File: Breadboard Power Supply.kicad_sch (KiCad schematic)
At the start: 28 parts, among them J1 USB-C, J10 Conn_01x02_Male, J11 Conn_01x02_Male, J2 Conn_02x03_Odd_Even, J3 Conn_02x03_Odd_Even, J8 Conn_01x02_Male, J9 Conn_01x02_Male, U1 LM1117DT-ADJ, U2 LM1117DT-ADJ

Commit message: Updated potentiometer part number.
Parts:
- RV1, RV2: Digi-Key Part Num (none) -> 563-ST4ETB102CT-ND; Manufacturer (none) -> Nidec; Mfg Part Num (none) -> ST-4ETB102
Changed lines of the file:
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@@
       (effects (font (size 1.27 1.27)) hide)
     )
-    (property "Datasheet" "~" (at 97.79 106.68 0)
-      (effects (font (size 1.27 1.27)) hide)
+    (property "Datasheet" "https://www.nidec-components.com/e/catalog/trimmer/st-4.pdf" (at 97.79 106.68 0)
+      (effects (font (size 1.27 1.27)) hide)
+    )
+    (property "Manufacturer" "Nidec" (at 97.79 106.68 0)
+      (effects (font (size 1.27 1.27)) hide)
+    )
+    (property "Mfg Part Num" "ST-4ETB102" (at 97.79 106.68 0)
+      (effects (font (size 1.27 1.27)) hide)
+    )
+    (property "Digi-Key Part Num" "563-ST4ETB102CT-ND" (at 97.79 106.68 0)
+      (effects (font (size 1.27 1.27)) hide)
+    )
+    (property "Description" "" (at 97.79 106.68 0)
+      (effects (font (size 1.27 1.27)))
     )
     (pin "1")
@@
       (effects (font (size 1.27 1.27)) hide)
     )
-    (property "Datasheet" "~" (at 97.79 151.13 0)
-      (effects (font (size 1.27 1.27)) hide)
-    )
-    (pin "1")
+    (property "Datasheet" "https://www.nidec-components.com/e/catalog/trimmer/st-4.pdf" (at 97.79 151.13 0)
+      (effects (font (size 1.27 1.27)) hide)
+    )
+    (property "Manufacturer" "Nidec" (at 97.79 151.13 0)
+      (effects (font (size 1.27 1.27)) hide)
+    )
+    (property "Mfg Part Num" "ST-4ETB102" (at 97.79 151.13 0)
+      (effects (font (size 1.27 1.27)) hide)
+    )
+    (property "Digi-Key Part Num" "563-ST4ETB102CT-ND" (at 97.79 151.13 0)
+      (effects (font (size 1.27 1.27)) hide)
+    )
+    (property "Description" "" (at 97.79 151.13 0)
+      (effects (font (size 1.27 1.27)))
+    )
+    (pin "1")

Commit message: Got rid of To Do list.
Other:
- note removed: "To Do 1) XXX Move the R1 reference designator away from the USB-C mounting hole. 2) XXX Use variable voltage regulators. 3) XXX Update version numbers. 4) XXX Get rid of local libraries. 5) XXX Doublecheck fill areas. 6) Finish mechanical changes. 7) XXX Change the order of the power headers. 8) XXX Get rid of the Zener diode. 9) XXX There's a via in the word Supply on the back silkscreen."
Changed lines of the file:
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@@
     (effects (font (size 1.27 1.27)) (justify left bottom))
-  )
-  (text "To Do\n\n1) XXX Move the R1 reference designator away from the USB-C mounting hole.\n2) XXX Use variable voltage regulators.\n3) XXX Update version numbers.\n4) XXX Get rid of local libraries.\n5) XXX Doublecheck fill areas.\n6) Finish mechanical changes.\n7) XXX Change the order of the power headers.\n8) XXX Get rid of the Zener diode.\n9) XXX There's a via in the word Supply on the back silkscreen."
-    (at 172.72 46.99 0)
-    (effects (font (size 1.27 1.27)) (justify left bottom) (href "#1"))
   )
   (text "5V Input" (at 50.8 24.765 0)

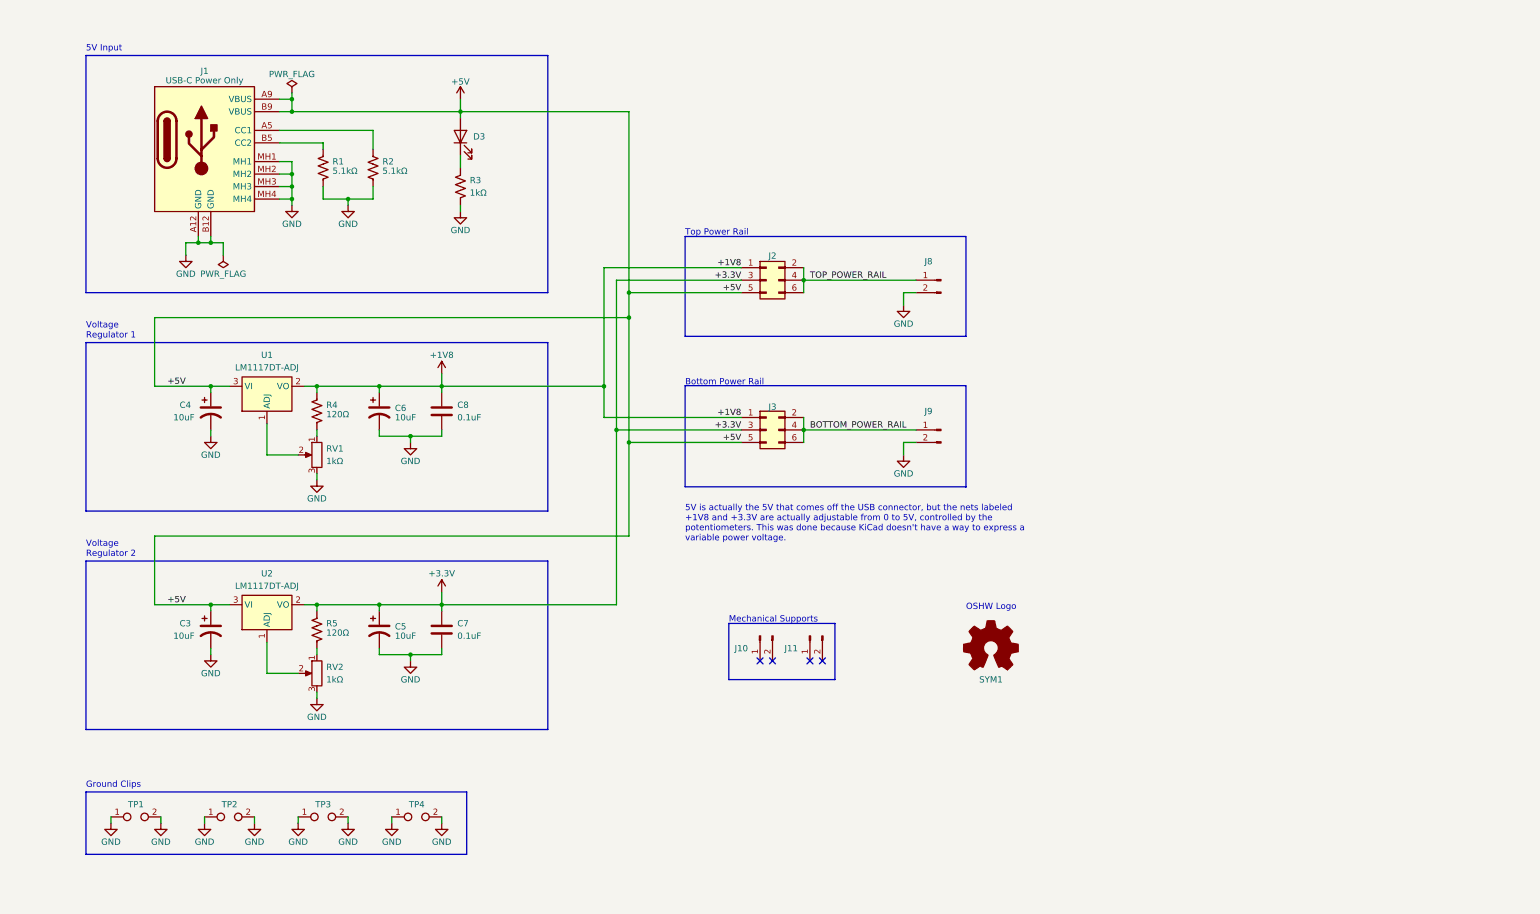
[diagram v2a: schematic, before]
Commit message: Redid schematic with both fixed and adjustable voltage regulators.
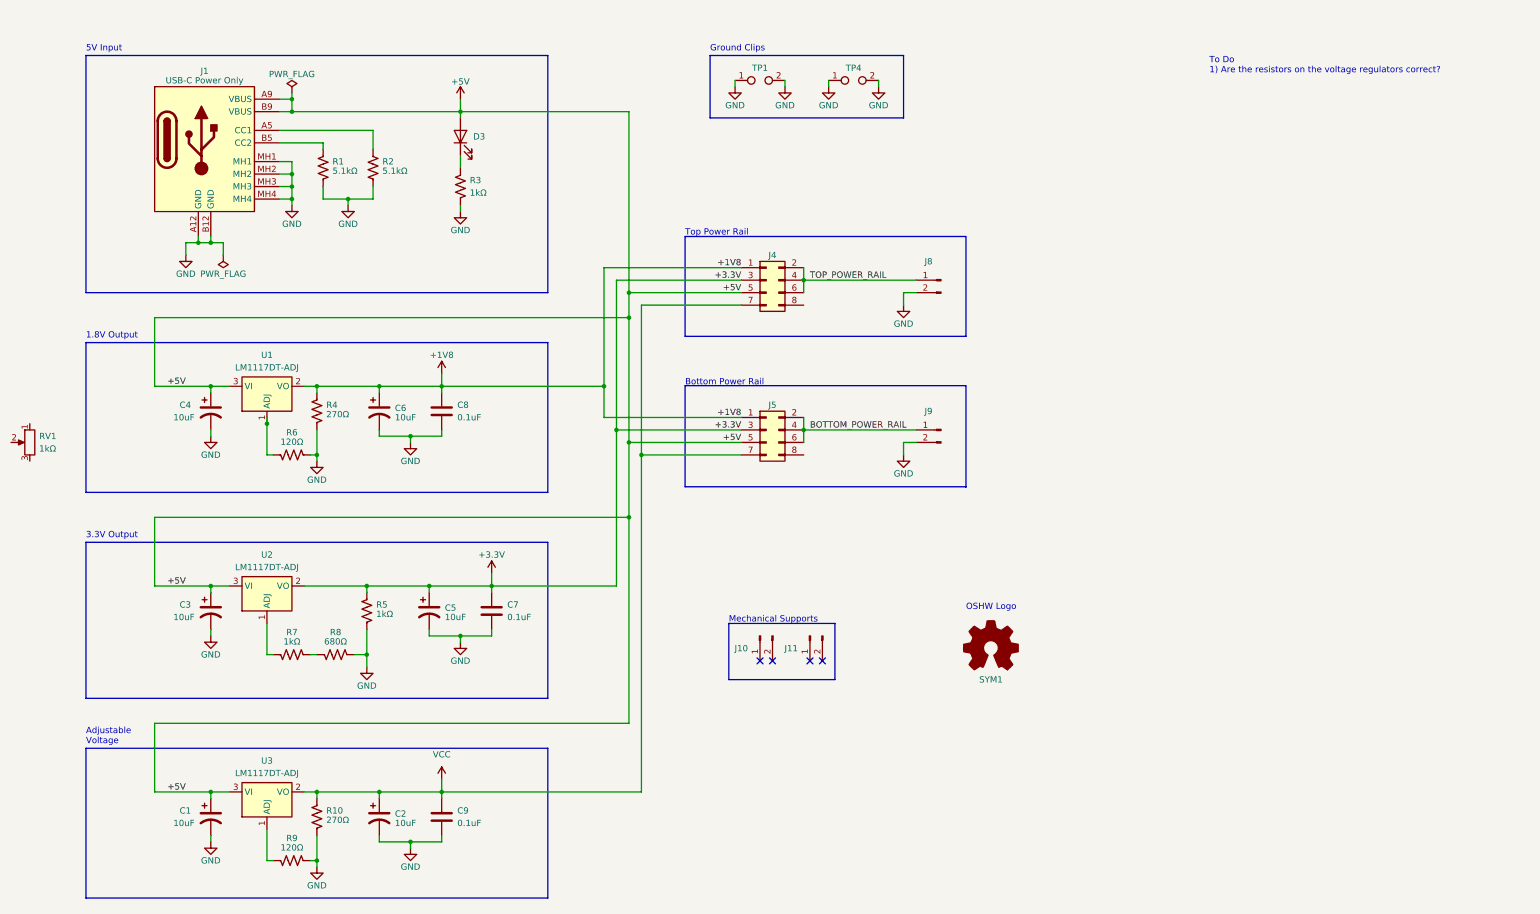
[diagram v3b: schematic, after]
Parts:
- removed J2, J3: Conn_02x03_Odd_Even, Connector_PinHeader_2.54mm:PinHeader_2x03_P2.54mm_Vertical, symbol Connector_Generic:Conn_02x03_Odd_Even
- removed RV2: 1kΩ, Local-Footprints:ST4ETB103 Potentiometer, symbol Device:R_Potentiometer
- removed TP2, TP3: TestPoint_2Pole, Global-Footprints:Keystone 1430, symbol Connector:TestPoint_2Pole
- added C1, C2: 10uF, Capacitor_SMD:C_0805_2012Metric, symbol Device:C_Polarized_US
- added C9: 0.1uF, Capacitor_SMD:C_0402_1005Metric, symbol Device:C
- added J4, J5: Conn_02x04_Odd_Even, Connector_PinHeader_2.54mm:PinHeader_2x04_P2.54mm_Vertical, symbol Connector_Generic:Conn_02x04_Odd_Even
- added R10: 270Ω, Resistor_SMD:R_0402_1005Metric, symbol Device:R_US
- added R6, R9: 120Ω, Resistor_SMD:R_0402_1005Metric, symbol Device:R_US
- added R7: 1kΩ, Resistor_SMD:R_0402_1005Metric, symbol Device:R_US
- added R8: 680Ω, Resistor_SMD:R_0402_1005Metric, symbol Device:R_US
- added U3: LM1117DT-ADJ, Package_TO_SOT_SMD:SOT-223-3_TabPin2, symbol Regulator_Linear:LM1117DT-ADJ
- R4: value 120Ω -> 270Ω
- R5: value 120Ω -> 1kΩ
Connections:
- net +1V8: now also J4.1 (Pin_1), J5.1 (Pin_1)
- net +3.3V: now also J4.3 (Pin_3), J5.3 (Pin_3)
- net +5V: now also C1.1, J4.5 (Pin_5), J5.5 (Pin_5), U3.3 (VI)
- net BOTTOM_POWER_RAIL: now also J5.2 (Pin_2), J5.4 (Pin_4), J5.6 (Pin_6)
- net GND: now also R4.2, R5.2, C1.2, C2.2, C9.2, R10.2, R6.2, R8.2, R9.2; no longer RV1.3
- net TOP_POWER_RAIL: now also J4.2 (Pin_2), J4.4 (Pin_4), J4.6 (Pin_6)
- net at RV1.1: no longer R4.2
- net at RV1.2: no longer U1.1 (ADJ)
- net at U2.1 (ADJ): now also R7.1
- new net: R6.1, U1.1 (ADJ)
- new net: R7.2, R8.1
- new net: R9.1, U3.1 (ADJ)
- new net VCC: C2.1, C9.1, J4.7 (Pin_7), J5.7 (Pin_7), R10.1, U3.2 (VO)
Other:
- note added: "1.8V Output"
- note added: "3.3V Output"
- note added: "Adjustable Voltage"
- note added: "To Do 1) Are the resistors on the voltage regulators correct?"
- note removed: "5V is actually the 5V that comes off the USB connector, but the nets labeled +1V8 and +3.3V are actually adjustable from 0 to 5V, controlled by the potentiometers. This was done because KiCad doesn't have a way to express a variable power voltage."
- note removed: "Voltage Regulator 1"
- note removed: "Voltage Regulator 2"
- moved on the sheet: C3, C5, C7, R5, RV1, TP1, TP4, U2

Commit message: Feature complete schematic.
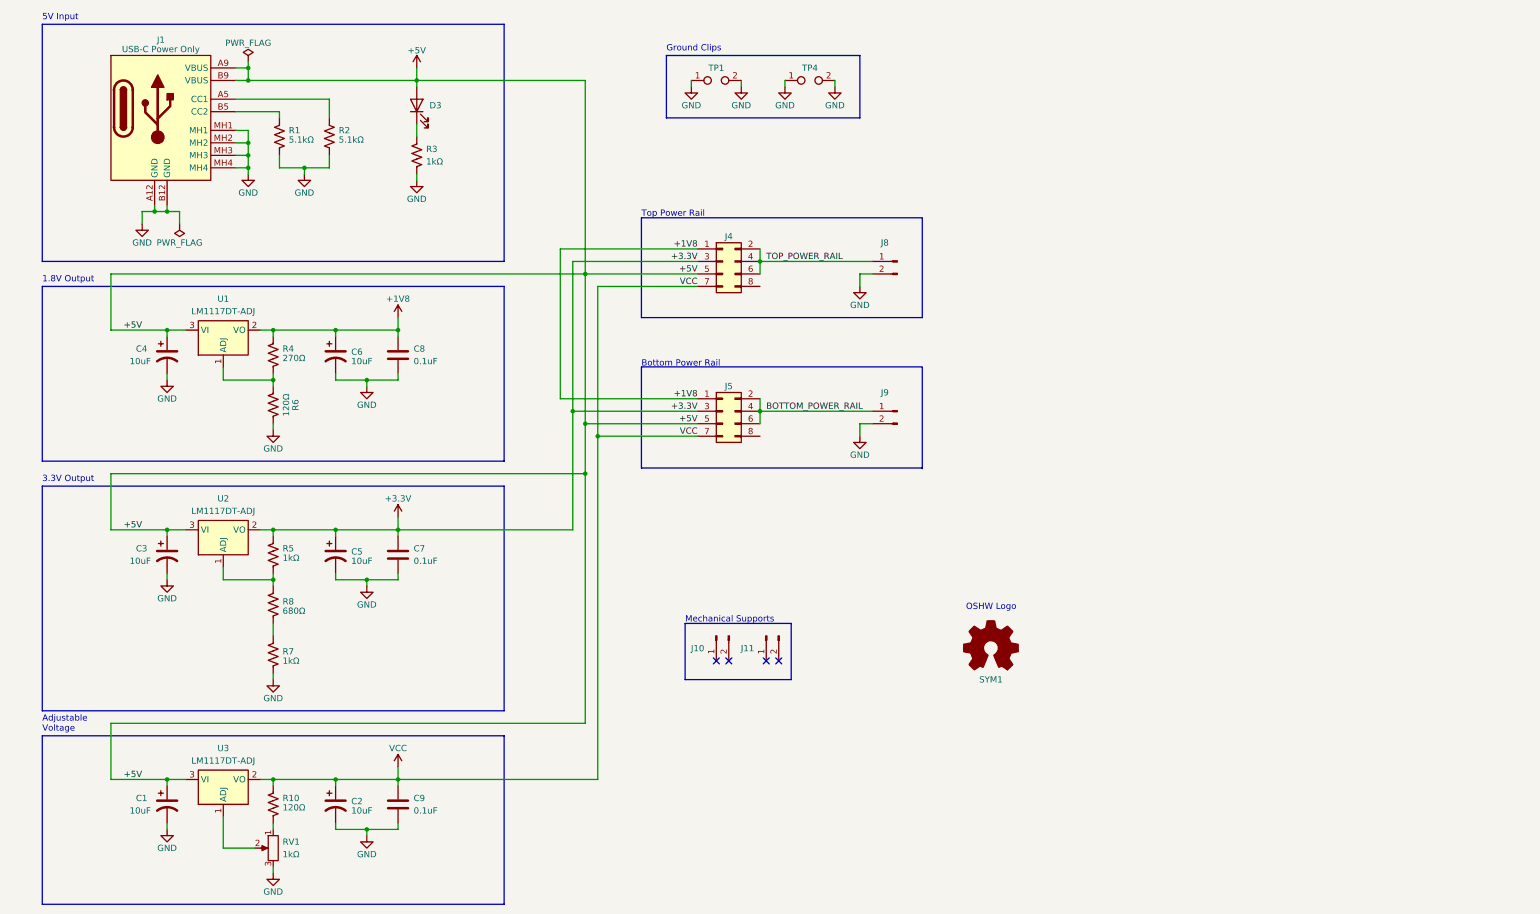
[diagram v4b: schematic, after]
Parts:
- removed R9: 120Ω, Resistor_SMD:R_0402_1005Metric, symbol Device:R_US
- R10: value 270Ω -> 120Ω
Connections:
- net GND: now also R7.2, RV1.3; no longer R10.2, R4.2, R5.2, R8.2
- net at RV1.1: now also R10.2
- net at RV1.2: now also U3.1 (ADJ)
- net at R6.1, U1.1 (ADJ): now also R4.2
- net at R7.1: now also R8.2; no longer U2.1 (ADJ)
- net at R8.1: now also R5.2, U2.1 (ADJ); no longer R7.2
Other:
- note removed: "To Do 1) Are the resistors on the voltage regulators correct?"
- moved on the sheet: C1, C2, C3, C4, C5, C6, C7, C8, C9, D3, J1, J10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

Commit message: Finished layout.
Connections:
- net +1V8: now also J5.2 (Pin_2); no longer J5.1 (Pin_1)
- net +3.3V: now also J5.4 (Pin_4); no longer J5.3 (Pin_3)
- net +5V: now also J5.6 (Pin_6); no longer J5.5 (Pin_5)
- net BOTTOM_POWER_RAIL: now also J5.1 (Pin_1), J5.3 (Pin_3), J5.5 (Pin_5), J5.7 (Pin_7); no longer J5.2 (Pin_2), J5.4 (Pin_4), J5.6 (Pin_6)
- net GND: now also J10.1 (Pin_1), J10.2 (Pin_2), J11.1 (Pin_1), J11.2 (Pin_2)
- net TOP_POWER_RAIL: now also J4.8 (Pin_8)
- net VCC: now also J5.8 (Pin_8); no longer J5.7 (Pin_7)
- no-connect marks 4 -> 0
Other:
- note added: "To Do 1) Update version numbers."
- moved on the sheet: J8, J9

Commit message: Updated version numbers.
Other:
- note added: "To Do 1) XXX Update version numbers."
- note removed: "To Do 1) Update version numbers."
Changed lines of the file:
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@@
   (title_block
     (title "Breadboard Power Supply")
-    (date "2023-06-28")
-    (rev "v10")
+    (date "2023-07-18")
+    (rev "v11")
   )
   (junction (at 154.94 102.87) (diameter 0) (color 0 0 0 0)
@@
     (effects (font (size 1.27 1.27)) (justify left bottom))
   )
-  (text "To Do\n\n1) Update version numbers." (at 222.25 26.035 0)
+  (text "To Do\n\n1) XXX Update version numbers." (at 222.25 26.035 0)
     (effects (font (size 1.27 1.27)) (justify left bottom))
   )

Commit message: Generated Gerber files.
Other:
- note removed: "To Do 1) XXX Update version numbers."
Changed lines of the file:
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@@
-    (effects (font (size 1.27 1.27)) (justify left bottom))
-  )
-  (text "To Do\n\n1) XXX Update version numbers." (at 222.25 26.035 0)
     (effects (font (size 1.27 1.27)) (justify left bottom))
   )

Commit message: Feedback from first prototype.
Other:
- note added: "To Do 1) Delete C4 reference designator. 2) Delete J4 reference designator. 3) Put + and - on the front silkscreen."
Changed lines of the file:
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@@
+    (effects (font (size 1.27 1.27)) (justify left bottom))
+  )
+  (text "To Do\n\n1) Delete C4 reference designator.\n2) Delete J4 reference designator.\n3) Put + and - on the front silkscreen."
+    (at 220.98 31.75 0)
     (effects (font (size 1.27 1.27)) (justify left bottom))
   )
